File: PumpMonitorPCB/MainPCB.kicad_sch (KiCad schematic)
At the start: 9 parts, among them J4 Mains terminals, SW3 EN, SW4 BOOT, U4 ESP32-C6-WROOM-1U-N8

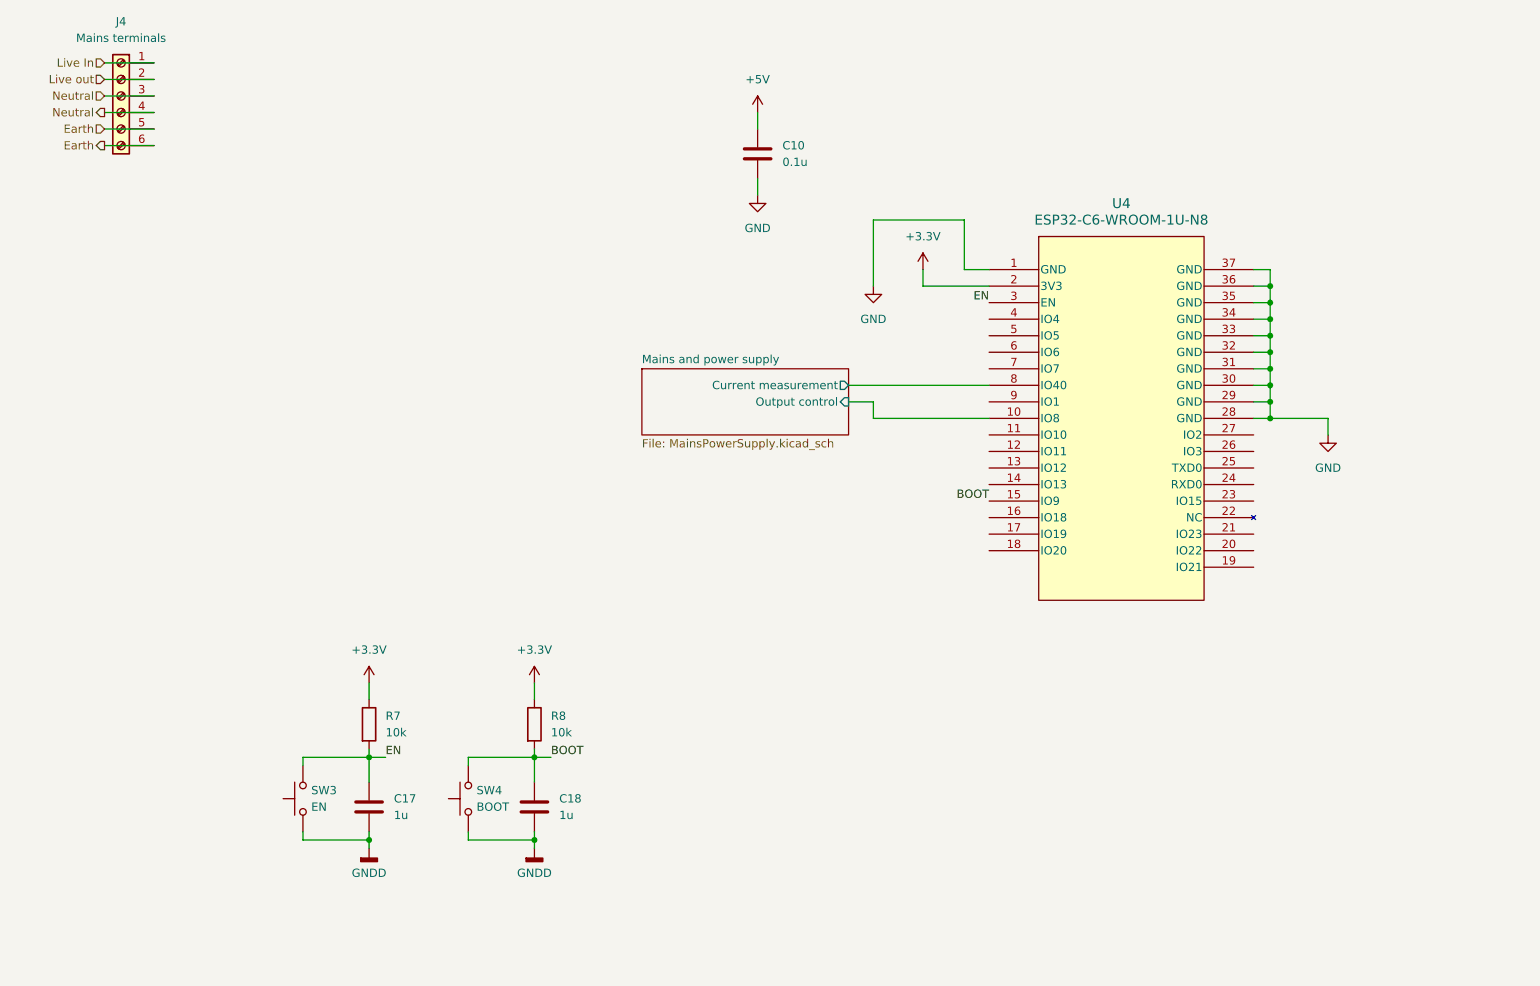
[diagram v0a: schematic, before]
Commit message: Adding microcontroller, USB, UI components.
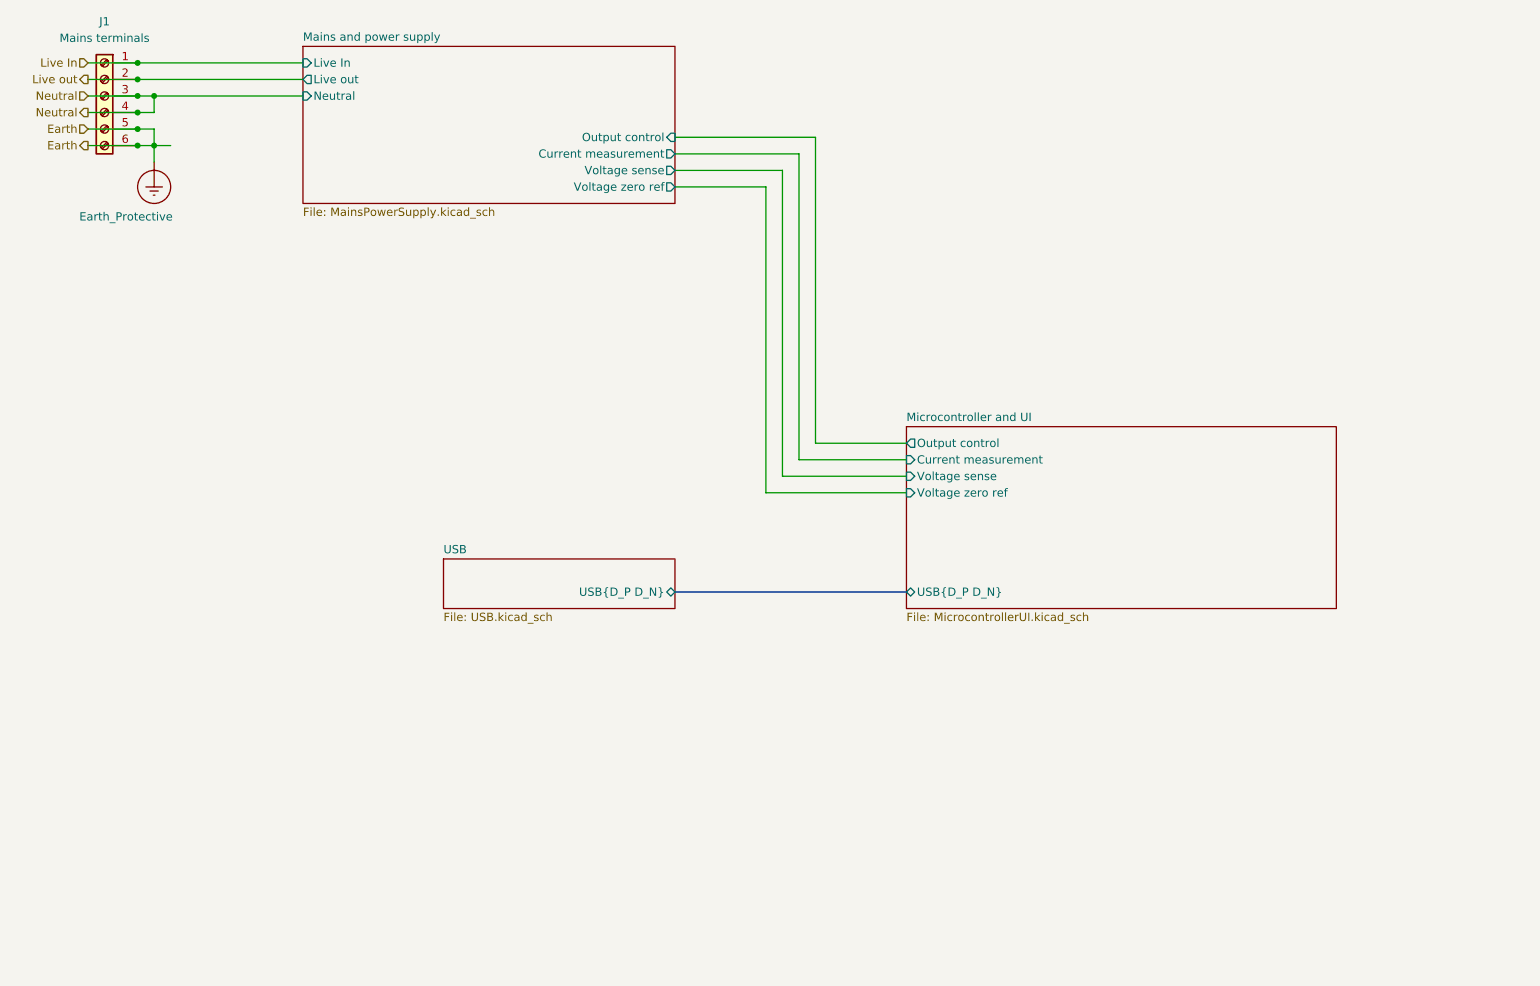
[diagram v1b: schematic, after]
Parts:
- removed C10: 0.1u, symbol Device:C
- removed C17, C18: 1u, Capacitor_SMD:C_0603_1608Metric_Pad1.08x0.95mm_HandSolder, symbol Device:C
- removed R7, R8: 10k, Resistor_SMD:R_0603_1608Metric_Pad0.98x0.95mm_HandSolder, symbol Device:R
- removed SW3: EN, Button_Switch_SMD:SW_Push_1P1T_NO_CK_KMR2, symbol Switch:SW_Push
- removed SW4: BOOT, Button_Switch_SMD:SW_Push_1P1T_NO_CK_KMR2, symbol Switch:SW_Push
- removed U4: ESP32-C6-WROOM-1U-N8, ESP32_C6_WROOM_1U_N8:MOD28_ESP32-C6-WROOM-1U_EXP, symbol ESP32_C6_WROOM_1U_N8:ESP32-C6-WROOM-1U-N8
- renumbered J4 to J1
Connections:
- net Earth renamed Earth_Protective
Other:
- added sheet Microcontroller and UI (MicrocontrollerUI.kicad_sch)
- added sheet USB (USB.kicad_sch)
- sheet Mains and power supply ports: added Live In, Live out, Neutral, Voltage sense, Voltage zero ref; removed none
- title: (none) -> Pump monitor - PCB
- moved on the sheet: J1

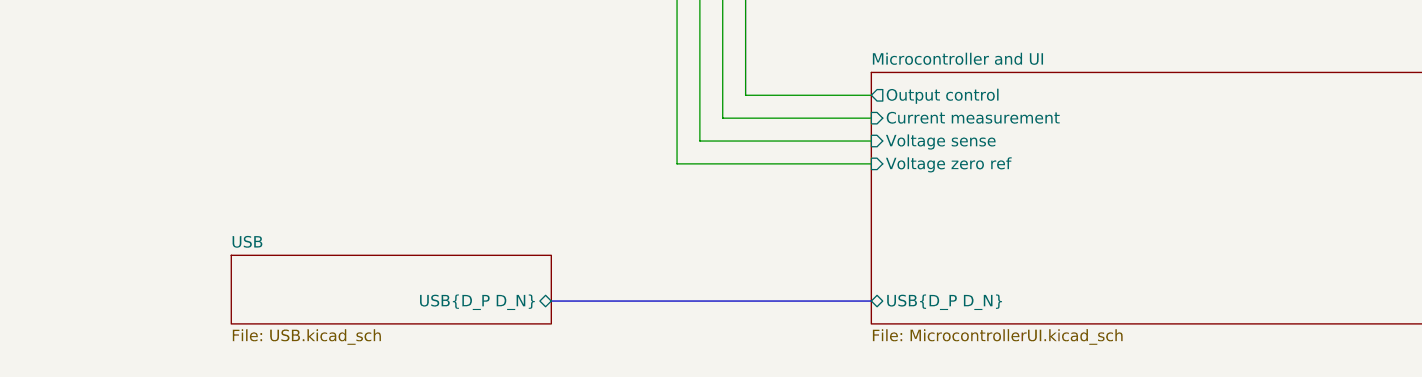
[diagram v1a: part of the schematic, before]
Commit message: Tidied schematic, added LoRa module.
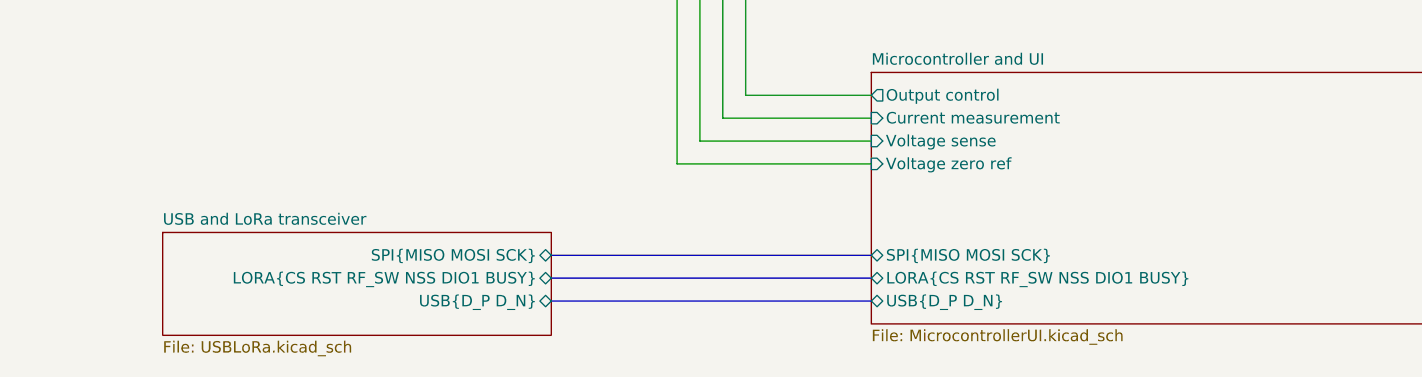
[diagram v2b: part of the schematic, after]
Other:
- sheet USB renamed USB and LoRa transceiver
- sheet Microcontroller and UI ports: added LORA{CS RST RF_SW NSS DIO1 BUSY}, SPI{MISO MOSI SCK}; removed none
- sheet USB and LoRa transceiver: file USB.kicad_sch -> USBLoRa.kicad_sch
- sheet USB and LoRa transceiver ports: added LORA{CS RST RF_SW NSS DIO1 BUSY}, SPI{MISO MOSI SCK}; removed none
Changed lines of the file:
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@@
 	(title_block
 		(title "Pump monitor - PCB")
-		(date "2025-09-16")
+		(date "2025-09-25")
 		(rev "V0.0.0")
 		(company "Jotham Gates")
@@
 		)
 	)
+	(bus
+		(pts
+			(xy 116.84 110.49) (xy 152.4 110.49)
+		)
+		(stroke
+			(width 0)
+			(type default)
+		)
+	)
 	(wire
 		(pts
 			(xy 36.83 39.37) (xy 34.29 39.37)
+		)
+		(stroke
+			(width 0)
+			(type default)
+		)
+	)
+	(bus
+		(pts
+			(xy 116.84 107.95) (xy 152.4 107.95)
 		)
 		(stroke
@@
 			)
 		)
+		(pin "LORA{CS RST RF_SW NSS DIO1 BUSY}" bidirectional
+			(at 152.4 110.49 180)
+			(effects
+				(font
+					(size 1.27 1.27)
+				)
+				(justify left)
+			)
+		)
+		(pin "SPI{MISO MOSI SCK}" bidirectional
+			(at 152.4 107.95 180)
+			(effects
+				(font
+					(size 1.27 1.27)
+				)
+				(justify left)
+			)
+		)
 		(instances
 			(project "PumpMonitorPCB"
@@
 	)
 	(sheet
-		(at 81.28 107.95)
-		(size 35.56 7.62)
+		(at 73.66 105.41)
+		(size 43.18 11.43)
 		(exclude_from_sim no)
 		(in_bom yes)
@@
 			(color 0 0 0 0.0000)
 		)
-		(property "Sheetname" "USB"
-			(at 81.28 107.2384 0)
+		(property "Sheetname" "USB and LoRa transceiver"
+			(at 73.66 104.6984 0)
 			(effects
 				(font
@@
 			)
 		)
-		(property "Sheetfile" "USB.kicad_sch"
-			(at 81.28 116.1546 0)
+		(property "Sheetfile" "USBLoRa.kicad_sch"
+			(at 73.66 117.4246 0)
 			(effects
 				(font
@@
 			(effects
 				(font
+					(size 1.27 1.27)
+				)
+				(justify right)
+			)
+		)
+		(pin "LORA{CS RST RF_SW NSS DIO1 BUSY}" bidirectional
+			(at 116.84 110.49 0)
+			(effects
+				(font
+					(size 1.27 1.27)
+				)
+				(justify right)
+			)
+		)
+		(pin "SPI{MISO MOSI SCK}" bidirectional
+			(at 116.84 107.95 0)
+			(effects
+				(font

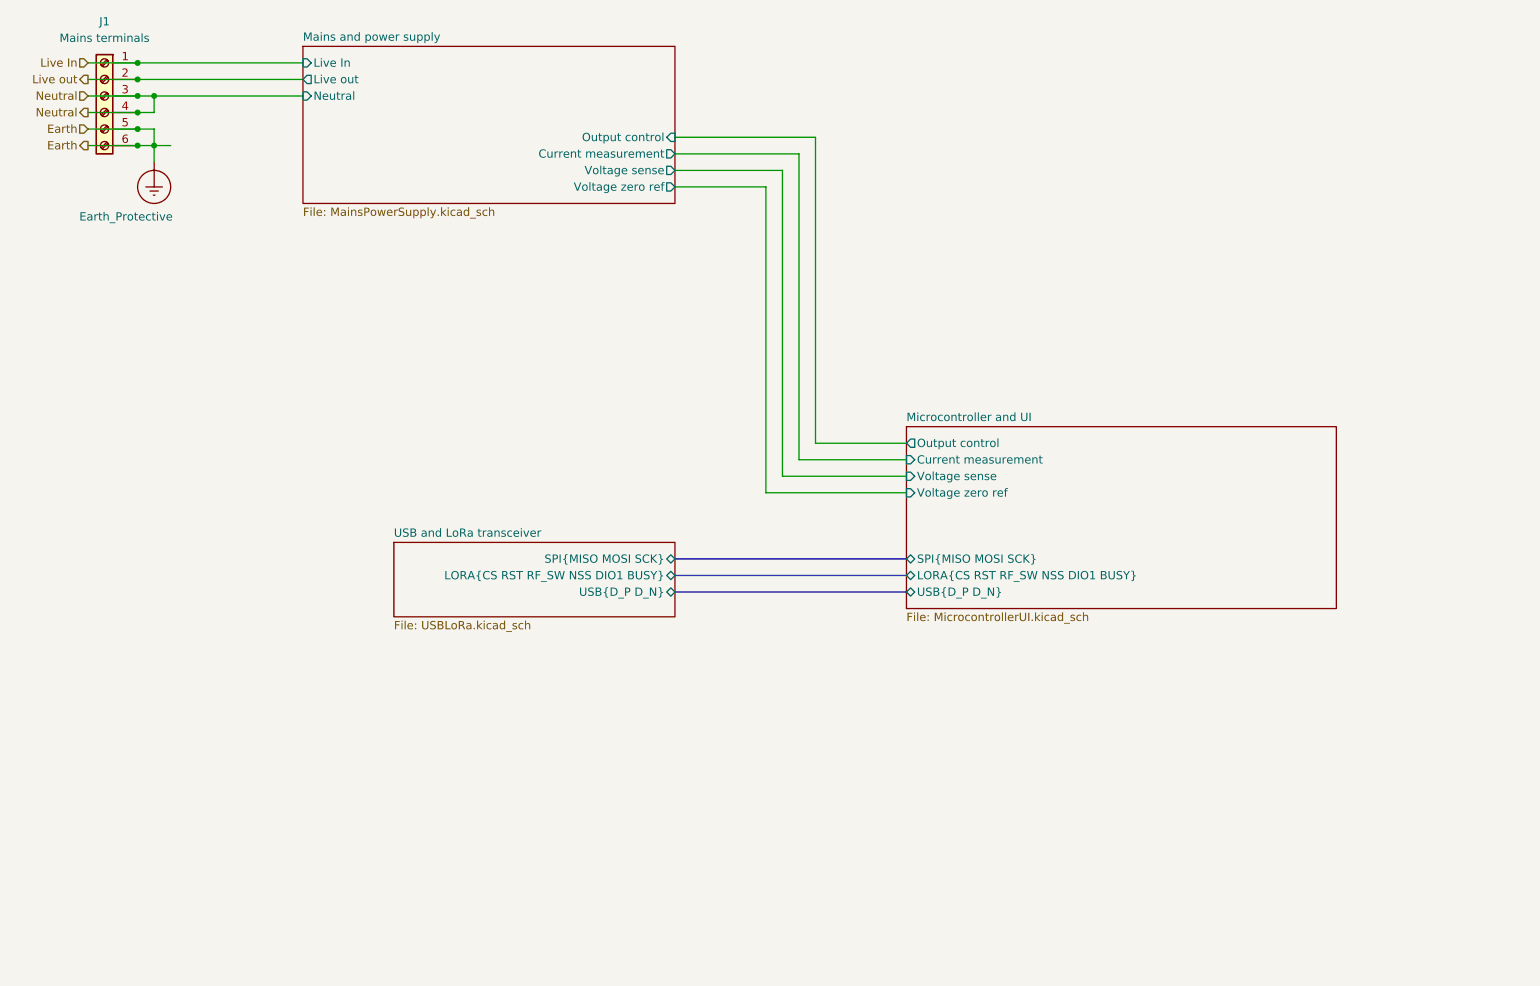
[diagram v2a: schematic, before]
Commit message: Added aux. connectors, started assigning components.
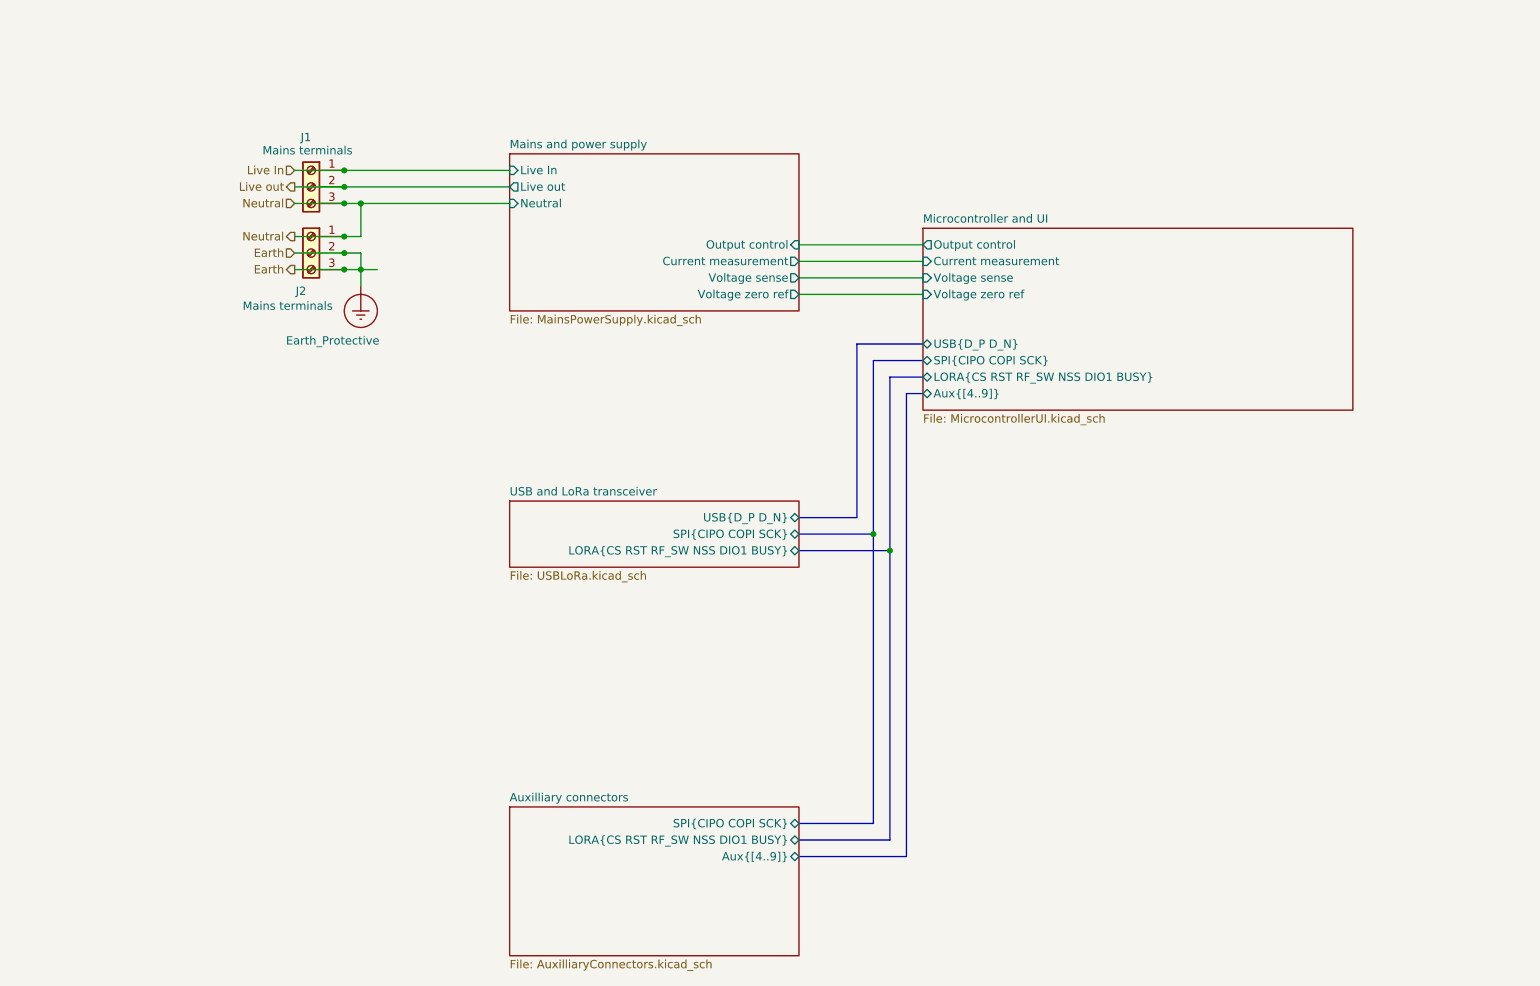
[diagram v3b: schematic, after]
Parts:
- removed J1: Mains terminals, symbol Connector:Screw_Terminal_01x06
- added J1, J2: Mains terminals, symbol Connector:Screw_Terminal_01x03
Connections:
- net Earth_Protective: now also J2.2 (Pin_2), J2.3 (Pin_3)
- net Live In: now also J1.1 (Pin_1)
- net Live out: now also J1.2 (Pin_2)
- net Neutral: now also J1.3 (Pin_3), J2.1 (Pin_1)
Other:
- added sheet Auxilliary connectors (AuxilliaryConnectors.kicad_sch)
- sheet Microcontroller and UI ports: added Aux{[4..9]}, SPI{CIPO COPI SCK}; removed SPI{MISO MOSI SCK}
- sheet USB and LoRa transceiver ports: added SPI{CIPO COPI SCK}; removed SPI{MISO MOSI SCK}

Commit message: Added op amps to voltage and current measurement, more footprint assignments.
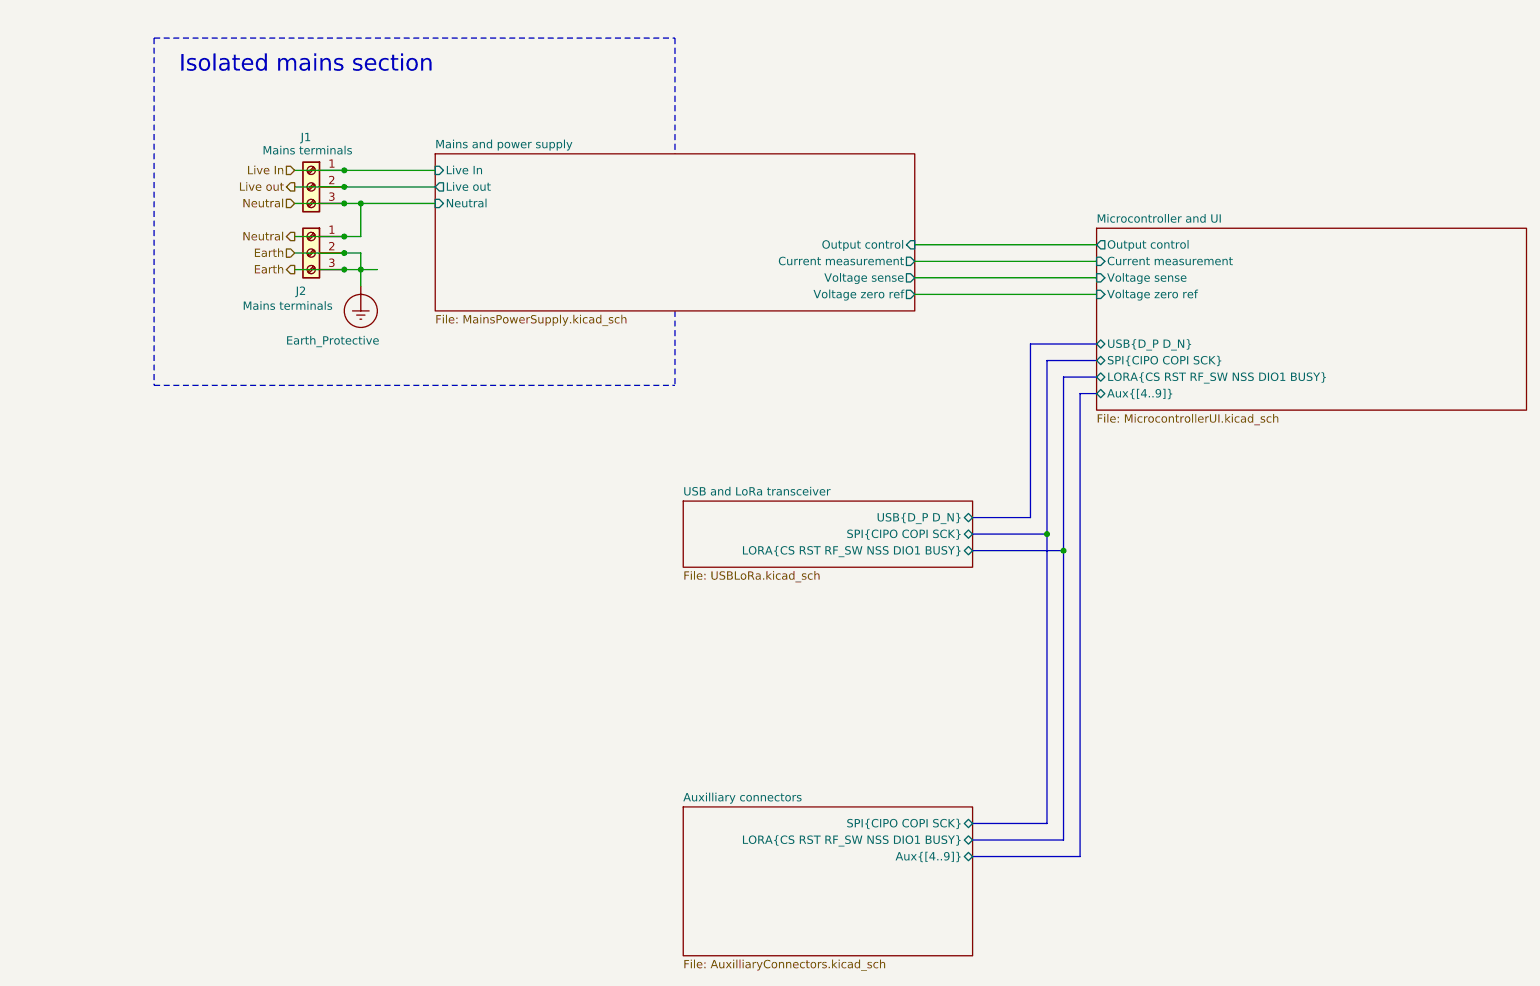
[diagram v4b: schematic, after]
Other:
- note added: "Isolated mains section"
